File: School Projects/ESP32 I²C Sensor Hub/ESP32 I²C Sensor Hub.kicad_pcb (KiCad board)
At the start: 2 copper layers, 49 parts, among them J3 Barrel_Jack, P1 USB_C_Plug_USB2.0, Q1 PMOS, Q2 PMOS, U1 ESP32-WROOM-32, U2 CP2102N-Axx-xQFN24, U3 AMS1117-3.3

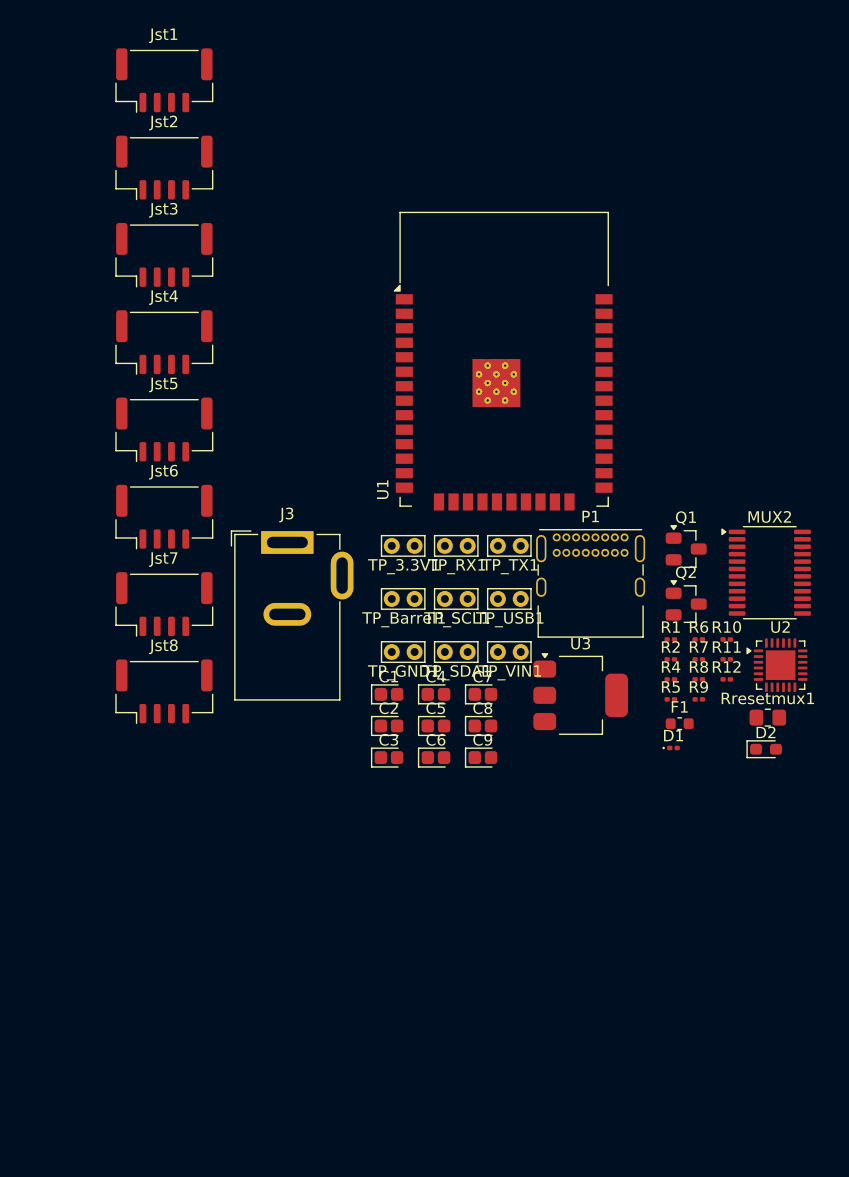
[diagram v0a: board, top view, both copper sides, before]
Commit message: Added final fab files for esp32 sensor port
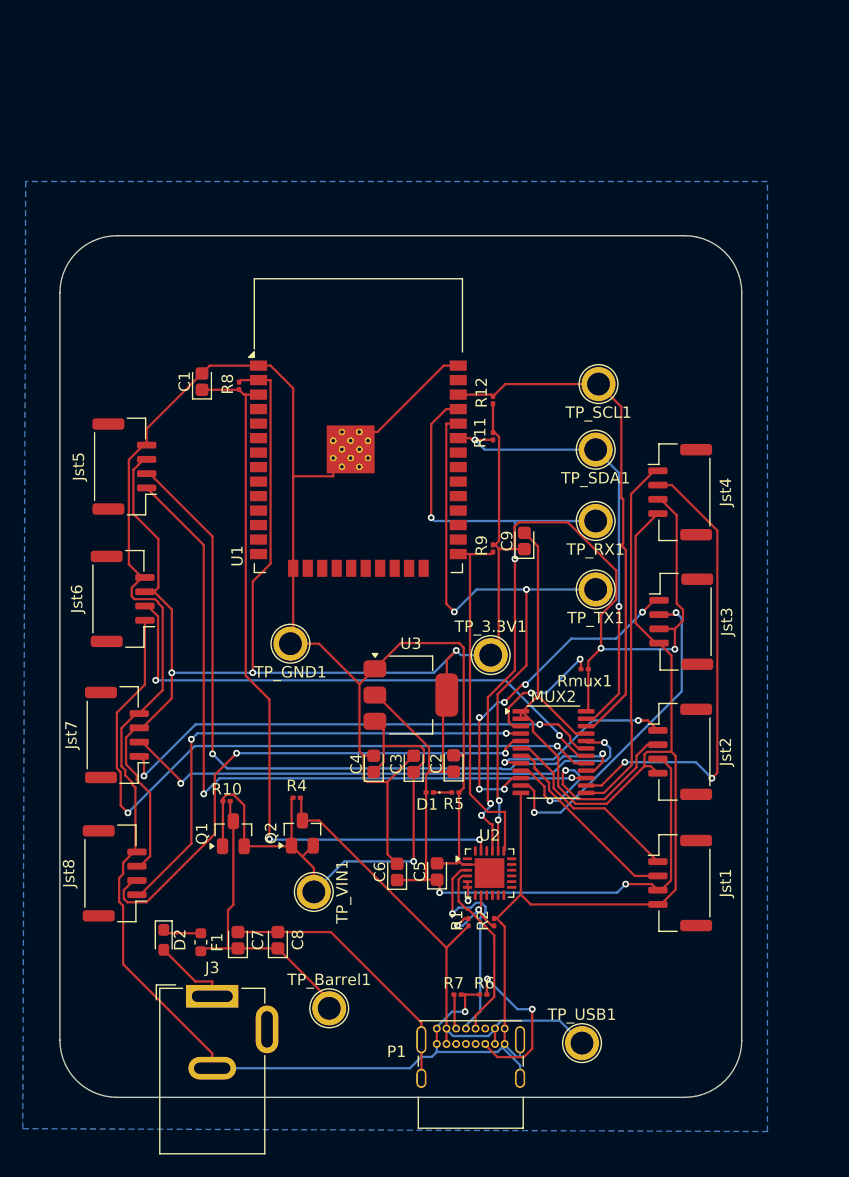
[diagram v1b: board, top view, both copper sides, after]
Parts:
- Rmux1: renamed from Rresetmux1; footprint Resistor_SMD:R_0805_2012Metric_Pad1.20x1.40mm_HandSolder -> Resistor_SMD:R_0201_0603Metric
- TP_3.3V1, TP_Barrel1, TP_GND1, TP_RX1, TP_SCL1, TP_SDA1, TP_TX1, TP_USB1, TP_VIN1: footprint TestPoint:TestPoint_Bridge_Pitch2.0mm_Drill0.7mm -> TestPoint:TestPoint_Plated_Hole_D2.0mm
- moved Jst1 83.6 mm to (159.8, 136.2), turned to -90 degrees
- moved Jst2 68.3 mm to (159.8, 124.7), turned to -90 degrees
- moved Jst3 55.5 mm to (159.9, 113.3), turned to -90 degrees
- moved D2 55.4 mm to (114.6, 141.2), turned to -90 degrees
- moved R8 47.8 mm to (121.2, 92.7), turned to -90 degrees
- moved Jst4 47.1 mm to (159.8, 102.0), turned to -90 degrees
- moved Q1 46.9 mm to (120.7, 131.9), turned to 90 degrees
- moved F1 46.1 mm to (117.8, 141.4), turned to -90 degrees
- moved R10 46.1 mm to (120.1, 129.1)
- moved P1 44.3 mm to (138.5, 149.0)
- moved J3 40.3 mm to (118.8, 146.2)
- moved TP_USB1 39.6 mm to (151.2, 150.2)
- moved Q2 39.2 mm to (126.8, 131.8), turned to 90 degrees
- moved R6 36.4 mm to (142.6, 146.0), turned to 180 degrees
- moved TP_Barrel1 36.3 mm to (129.1, 147.2)
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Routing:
- net GND: track 0.00 -> 391.2 mm, vias 0 -> 1
- net /Vcc3.3V_POWER: track 0.00 -> 245.5 mm, vias 0 -> 8
- net /SC5: track 0.00 -> 64.9 mm, vias 0 -> 2
- net /DTR_EN: track 0.00 -> 64.4 mm, vias 0 -> 2
- net /SD5: track 0.00 -> 63.0 mm, vias 0 -> 2
- net /SD6: track 0.00 -> 61.6 mm, vias 0 -> 2
- net /RX: track 0.00 -> 56.5 mm, vias 0 -> 4
- net /TX: track 0.00 -> 55.1 mm, vias 0 -> 4
- net /VREG_IN_POWER: track 0.00 -> 53.6 mm, vias 0 -> 1
- net /SC6: track 0.00 -> 47.8 mm, vias 0 -> 2
- net /SC7: track 0.00 -> 47.0 mm, vias 0 -> 2
- net /SC0: track 0.00 -> 46.3 mm, vias 0 -> 2
- net /SCL: track 0.00 -> 46.2 mm
- net /USB_POWER: track 0.00 -> 45.5 mm
- net /SD0: track 0.00 -> 44.9 mm, vias 0 -> 2
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- added copper zone on B.Cu, net GND
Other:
- board outline added: 59.8 x 75.5 mm
- board text added: "U3"
